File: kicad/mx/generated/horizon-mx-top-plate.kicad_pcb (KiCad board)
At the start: 2 copper layers, 38 x 38 mm, 5 parts

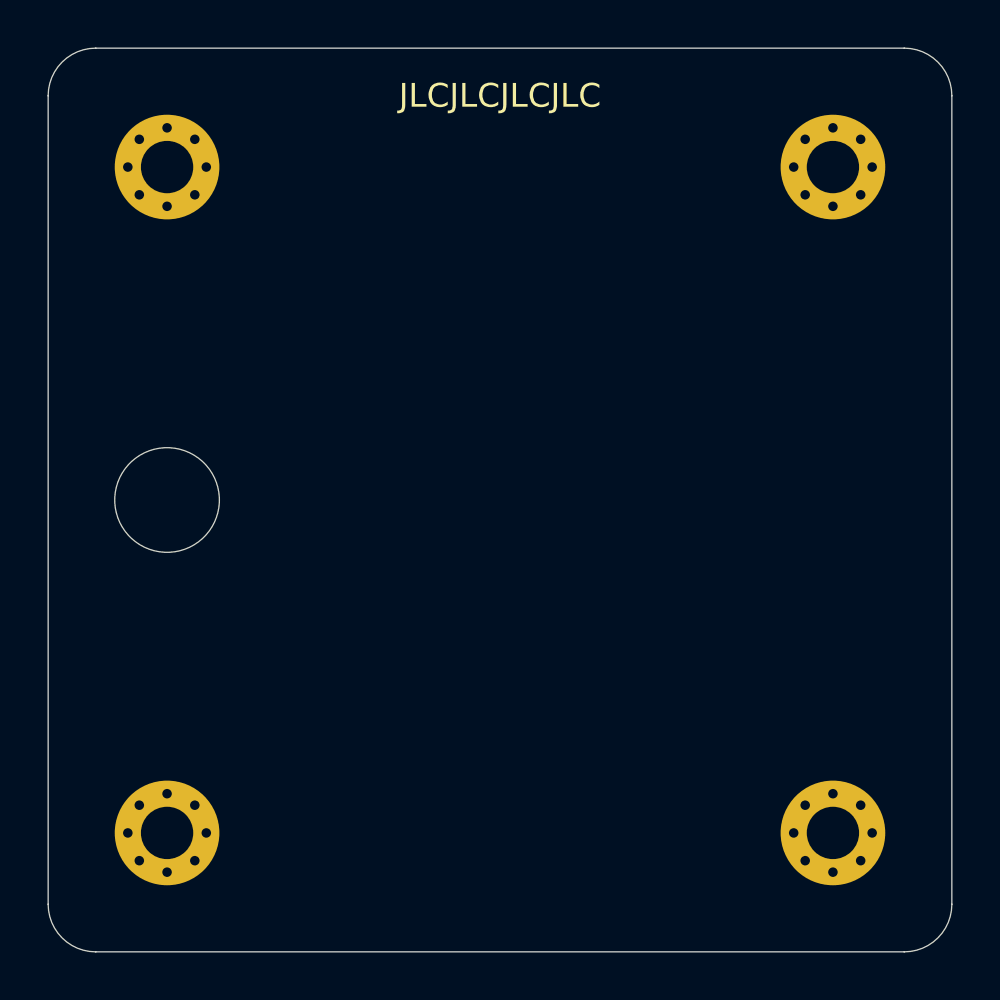
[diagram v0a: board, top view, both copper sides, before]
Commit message: Preserve logos on plate PCBs
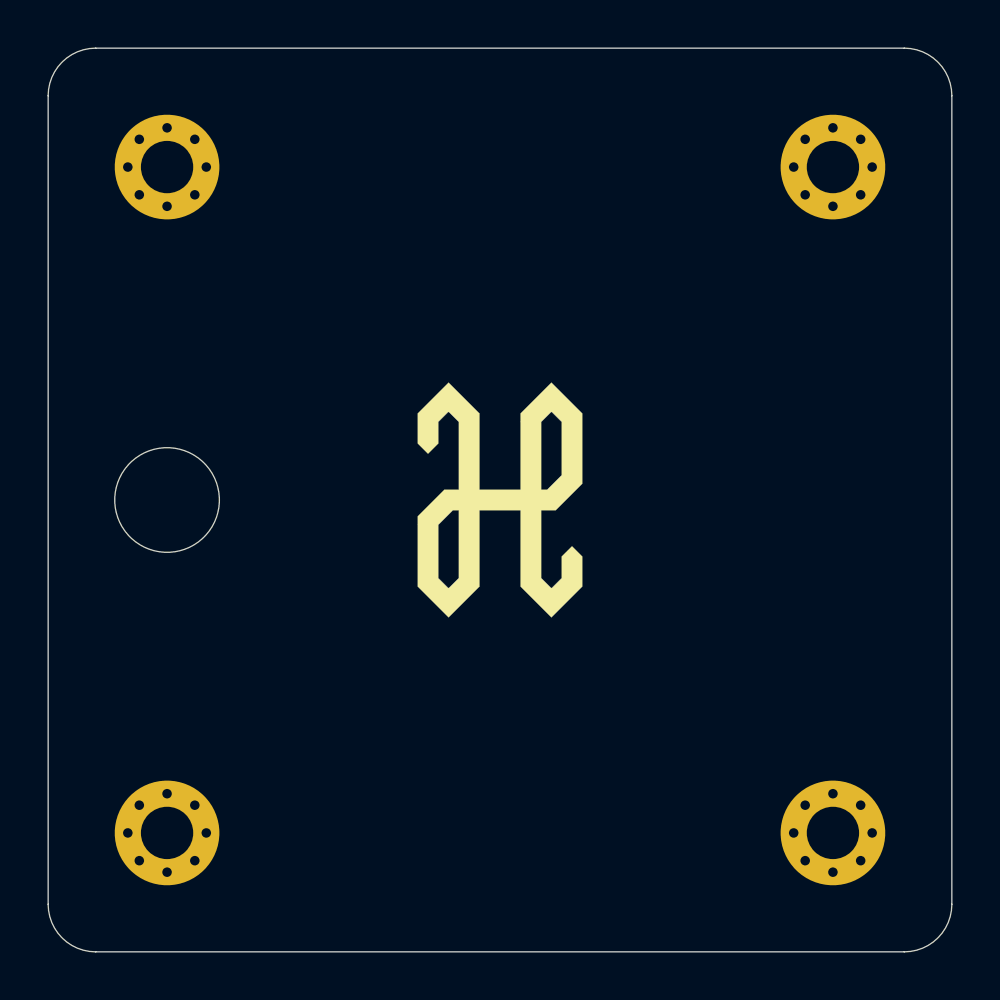
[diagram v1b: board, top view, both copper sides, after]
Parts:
- added ?: Logo-Top, horizon-footprints:Logo_Horizon_H, F.Cu at (209.0, 114.0)
- added ?: Logo-Bottom, horizon-footprints:Logo_Horizon_Small, B.Cu at (209.0, 100.5)
- added ?: PRO-MICRO, horizon-footprints:Pro-Micro, F.Cu at (209.0, 95.0)
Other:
- board text added: "github.com/skarrmann/horizon"
- board text added: "rev2 | MX"

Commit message: Remove unused footprints and other files. Update readme. Prepare for production!
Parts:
- moved ? 13.0 mm to (209.0, 113.5)
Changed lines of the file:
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@@
   )
   (module horizon-footprints:Logo_Horizon_Small (layer B.Cu)
-    (at 209 100.5 180)
+    (at 209 113.5 180)
     (fp_text reference "" (at 0 -2) (layer B.SilkS) hide
       (effects (font (size 1.524 1.524) (thickness 0.3)) (justify mirror))
@@
     (effects (font (size 1 1) (thickness 0.15)) (justify mirror))
   )
-  (gr_text "rev2 | MX" (at 209 104.5) (layer B.SilkS)
+  (gr_text "rev2 | MX" (at 209 117.5) (layer B.SilkS)
     (effects (font (size 1 1) (thickness 0.15)) (justify mirror))
   )
-  (gr_text JLCJLCJLCJLC (at 209 106.5) (layer B.SilkS)
+  (gr_text JLCJLCJLCJLC (at 209 131.5) (layer B.SilkS)
     (effects (font (size 1 1) (thickness 0.15)) (justify mirror))
   )
